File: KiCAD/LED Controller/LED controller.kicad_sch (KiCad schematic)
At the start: 41 parts, among them J1 Barrel_Jack_Switch, J2 4x RJ45, J3 Conn_01x24_Female, J4 Conn_01x24_Female, J5 8P8C_Shielded, SW1 ELUMOASAQ2C22, SW2 ELUMOASAQ2C22, SW3 ELUMOASAQ2C22, U1 SN75374D, U2 SN75374D, U3 Teensy4.1, U4 SN75374D, U5 SN74LV4053ADR, U6 DAC084S085CIMMX/NOPB, U7 NXB0104PWJ

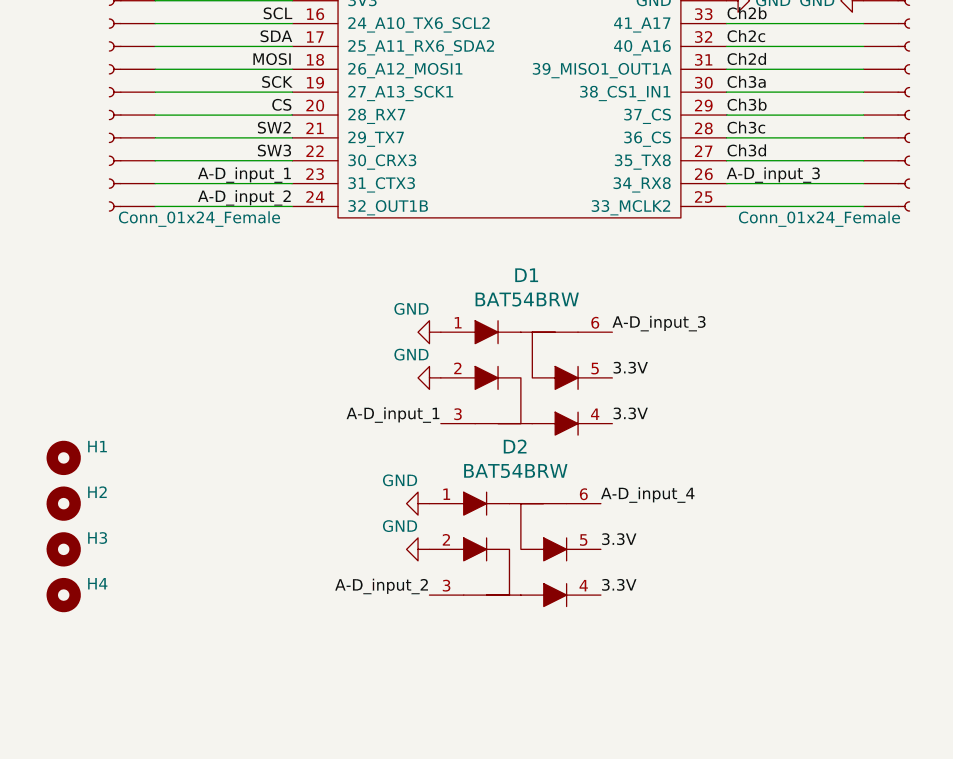
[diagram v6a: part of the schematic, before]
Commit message: All but caps connected
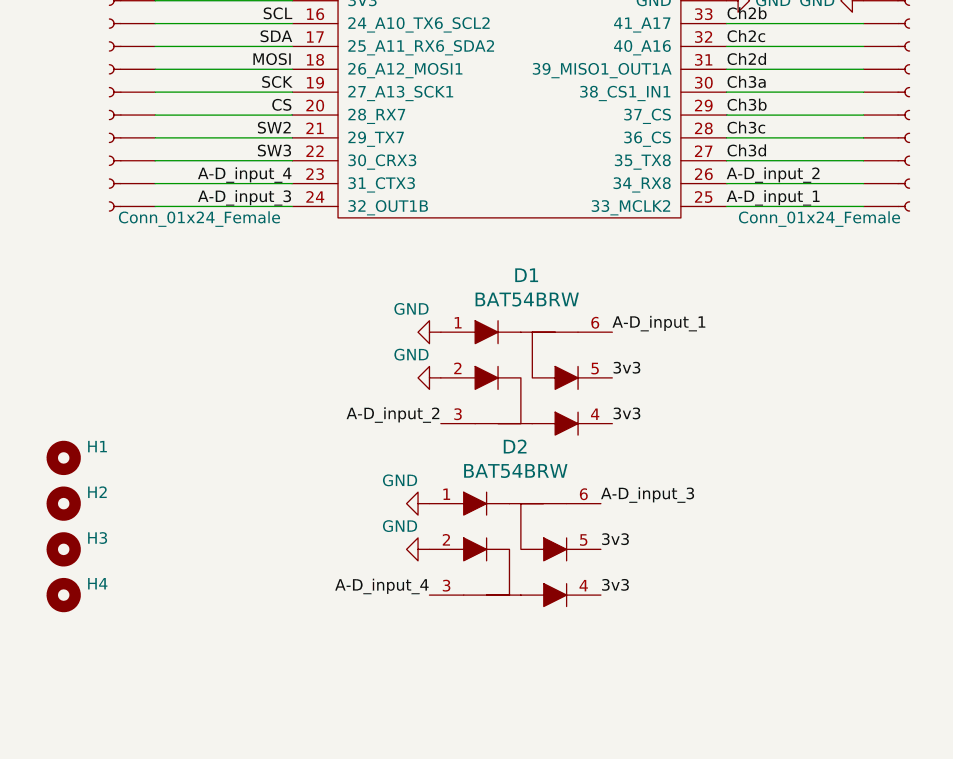
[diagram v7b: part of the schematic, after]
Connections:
- net 3.3V is gone; now on net 3v3: D1.4, D1.5, D2.4, D2.5
- net A-D_input_1: now also D1.6, J4.~, U3.25 (33_MCLK2); no longer D1.3, J3.~, U3.23 (31_CTX3)
- net A-D_input_2: now also D1.3, J4.~, U3.26 (34_RX8); no longer D2.3, J3.~, U3.24 (32_OUT1B)
- net A-D_input_3: now also D2.6, J3.~, U3.24 (32_OUT1B); no longer D1.6, J4.~, U3.26 (34_RX8)
- net A-D_input_4: now also D2.3, J3.~, U3.23 (31_CTX3); no longer D2.6
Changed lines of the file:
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@@
 	)
 	(label "A-D_input_1"
-		(at 219.71 123.19 180)
-		(fields_autoplaced yes)
-		(effects
-			(font
-				(size 1.27 1.27)
-			)
-			(justify right bottom)
+		(at 238.76 113.03 0)
+		(fields_autoplaced yes)
+		(effects
+			(font
+				(size 1.27 1.27)
+			)
+			(justify left bottom)
 		)
 	)
@@
 	)
 	(label "A-D_input_4"
-		(at 237.49 132.08 0)
-		(fields_autoplaced yes)
-		(effects
-			(font
-				(size 1.27 1.27)
-			)
-			(justify left bottom)
+		(at 218.44 142.24 180)
+		(fields_autoplaced yes)
+		(effects
+			(font
+				(size 1.27 1.27)
+			)
+			(justify right bottom)
 		)
 	)
@@
 	)
 	(label "A-D_input_1"
-		(at 203.2 96.52 180)
-		(fields_autoplaced yes)
-		(effects
-			(font
-				(size 1.27 1.27)
-			)
-			(justify right bottom)
+		(at 251.46 99.06 0)
+		(fields_autoplaced yes)
+		(effects
+			(font
+				(size 1.27 1.27)
+			)
+			(justify left bottom)
 		)
 	)
@@
 	)
 	(label "A-D_input_2"
-		(at 218.44 142.24 180)
+		(at 219.71 123.19 180)
 		(fields_autoplaced yes)
 		(effects
@@
 		)
 	)
-	(label "3.3V"
+	(label "3v3"
 		(at 238.76 123.19 0)
 		(fields_autoplaced yes)
@@
 	)
 	(label "A-D_input_2"
-		(at 203.2 99.06 180)
-		(fields_autoplaced yes)
-		(effects
-			(font
-				(size 1.27 1.27)
-			)
-			(justify right bottom)
+		(at 251.46 96.52 0)
+		(fields_autoplaced yes)
+		(effects
+			(font
+				(size 1.27 1.27)
+			)
+			(justify left bottom)
 		)
 	)
@@
 	)
 	(label "A-D_input_3"
-		(at 238.76 113.03 0)
+		(at 237.49 132.08 0)
 		(fields_autoplaced yes)
 		(effects
@@
 		)
 	)
-	(label "3.3V"
+	(label "3v3"
 		(at 238.76 118.11 0)
 		(fields_autoplaced yes)
@@
 		)
 	)
-	(label "3.3V"
+	(label "3v3"
 		(at 237.49 142.24 0)
 		(fields_autoplaced yes)
@@
 		)
 	)
-	(label "3.3V"
+	(label "3v3"
 		(at 237.49 137.16 0)
 		(fields_autoplaced yes)
@@
 		)
 	)
+	(label "A-D_input_4"
+		(at 203.2 96.52 180)
+		(fields_autoplaced yes)
+		(effects
+			(font
+				(size 1.27 1.27)
+			)
+			(justify right bottom)
+		)
+	)
 	(label "1-2"
 		(at 76.2 54.61 180)
@@
 	)
 	(label "A-D_input_3"
-		(at 251.46 96.52 0)
-		(fields_autoplaced yes)
-		(effects
-			(font
-				(size 1.27 1.27)
-			)
-			(justify left bottom)
-		)
-	)
+		(at 203.2 99.06 180)
+		(fields_autoplaced yes)
+		(effects
+			(font
+				(size 1.27 1.27)
+			)
+			(justify right bottom)
+		)
+	)

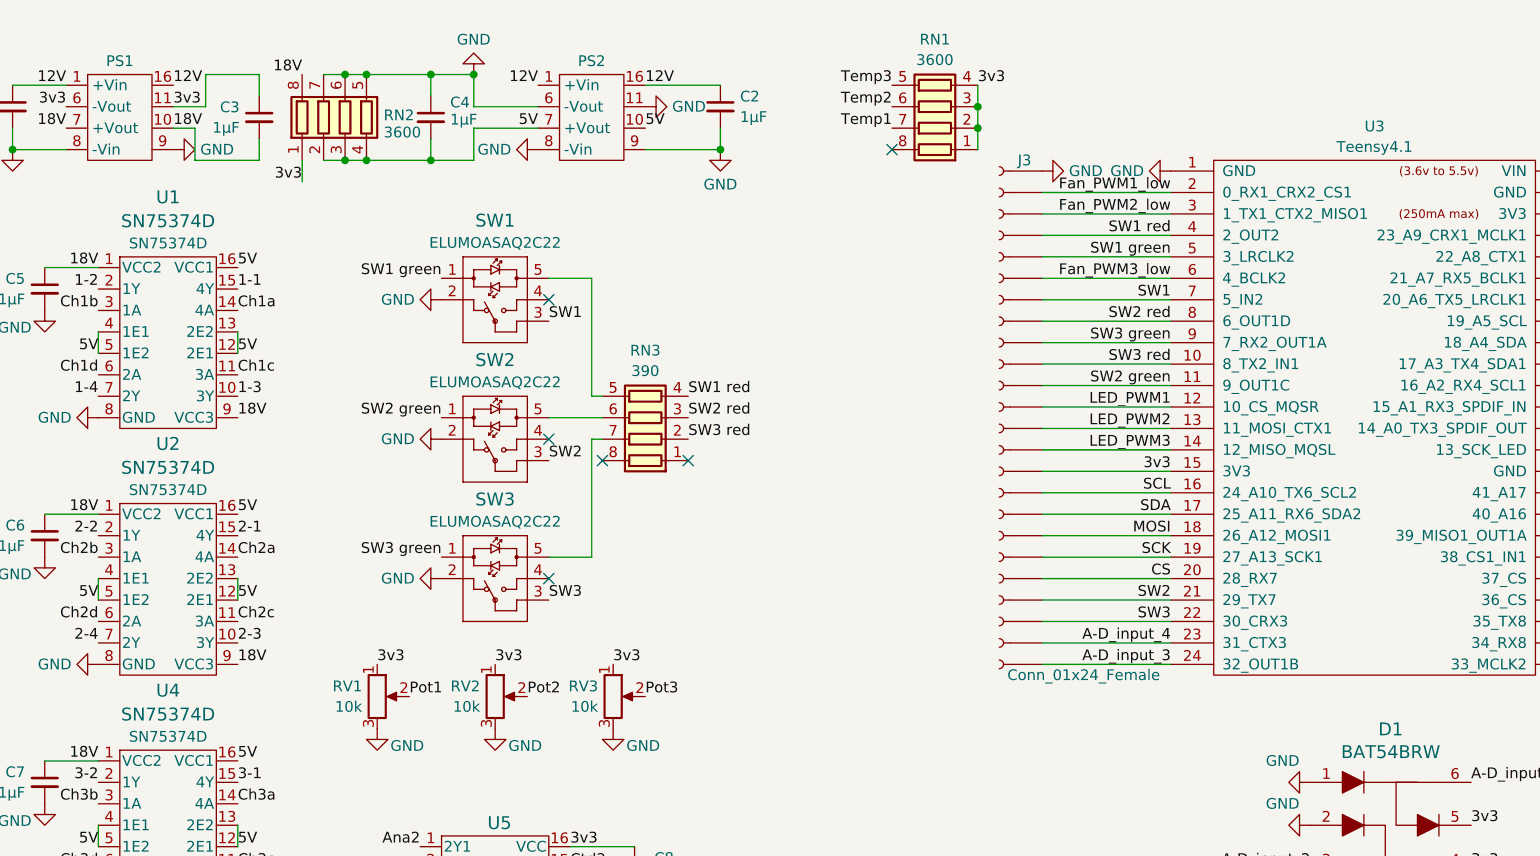
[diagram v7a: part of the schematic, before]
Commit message: All connected - pass DRC
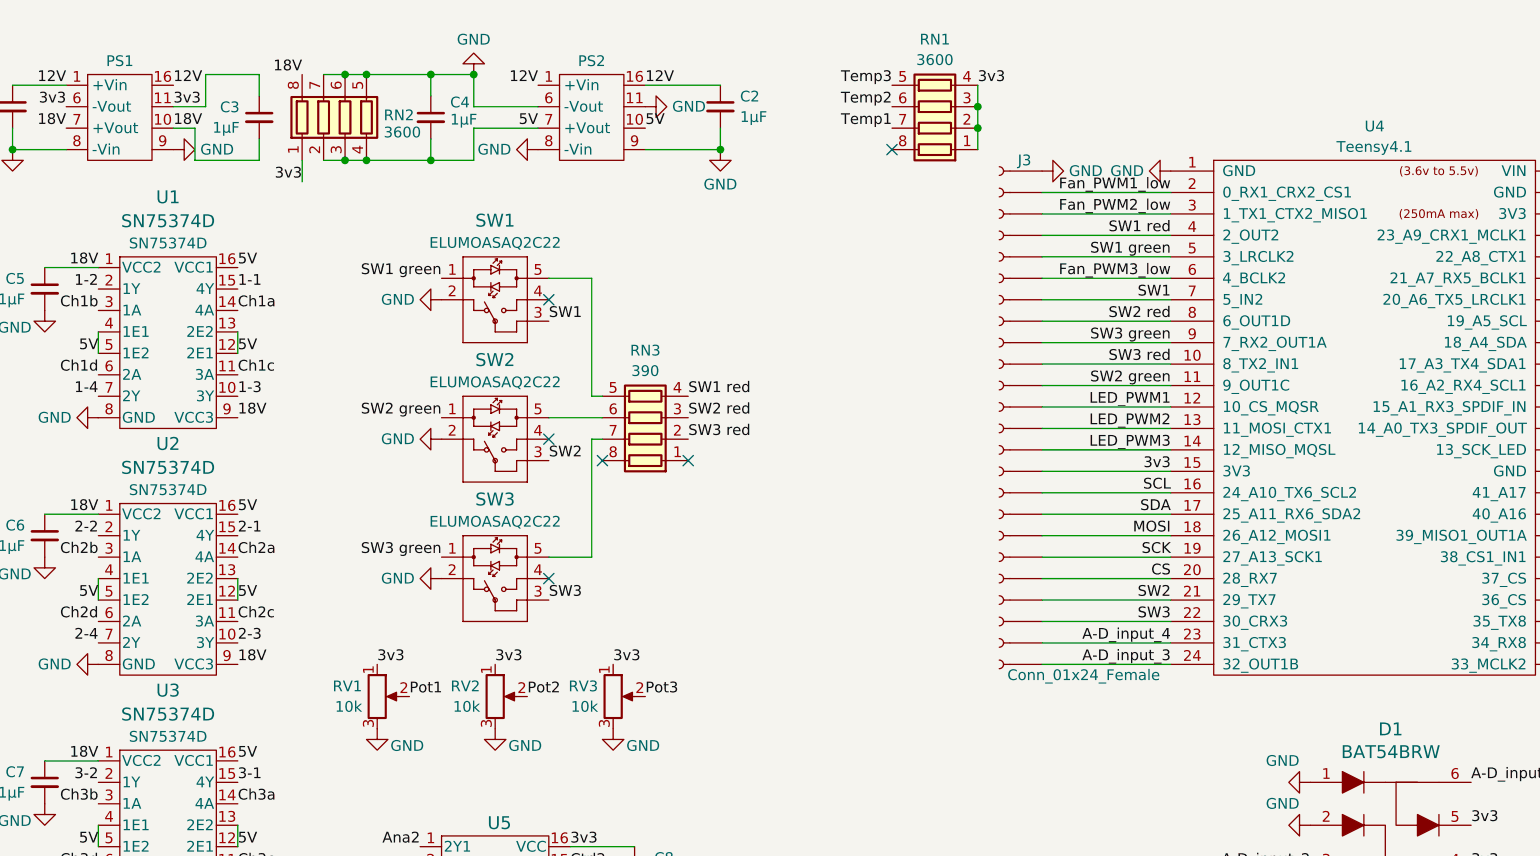
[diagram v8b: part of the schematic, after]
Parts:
- renumbered U4 to U3, U3 to U4
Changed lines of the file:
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@@
 	(wire
 		(pts
-			(xy 66.04 35.56) (xy 66.04 38.1)
-		)
-		(stroke
-			(width 0)
-			(type default)
-		)
-	)
-	(wire
-		(pts
 			(xy 53.34 147.32) (xy 54.61 147.32)
 		)
@@
 	(wire
 		(pts
+			(xy 66.04 35.56) (xy 66.04 38.1)
+		)
+		(stroke
+			(width 0)
+			(type default)
+		)
+	)
+	(wire
+		(pts
 			(xy 105.41 39.37) (xy 102.87 39.37)
 		)
@@
 		(dnp no)
 		(fields_autoplaced yes)
-		(property "Reference" "U4"
+		(property "Reference" "U3"
 			(at 84.455 102.1654 0)
 			(effects
@@
 			(project "LED controller"
 				(path "/7e3ae51b-fd56-44ae-a416-05dd2481d5ac"
-					(reference "U4")
+					(reference "U3")
 					(unit 1)
 				)
@@
 		(dnp no)
 		(fields_autoplaced yes)
-		(property "Reference" "U3"
+		(property "Reference" "U4"
 			(at 227.33 35.3525 0)
 			(effects
@@
 			(project ""
 				(path "/7e3ae51b-fd56-44ae-a416-05dd2481d5ac"
-					(reference "U3")
+					(reference "U4")
 					(unit 1)
 				)
